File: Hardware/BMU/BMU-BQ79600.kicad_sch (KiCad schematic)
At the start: 9 parts, among them U4 BQ79600PWRQ1

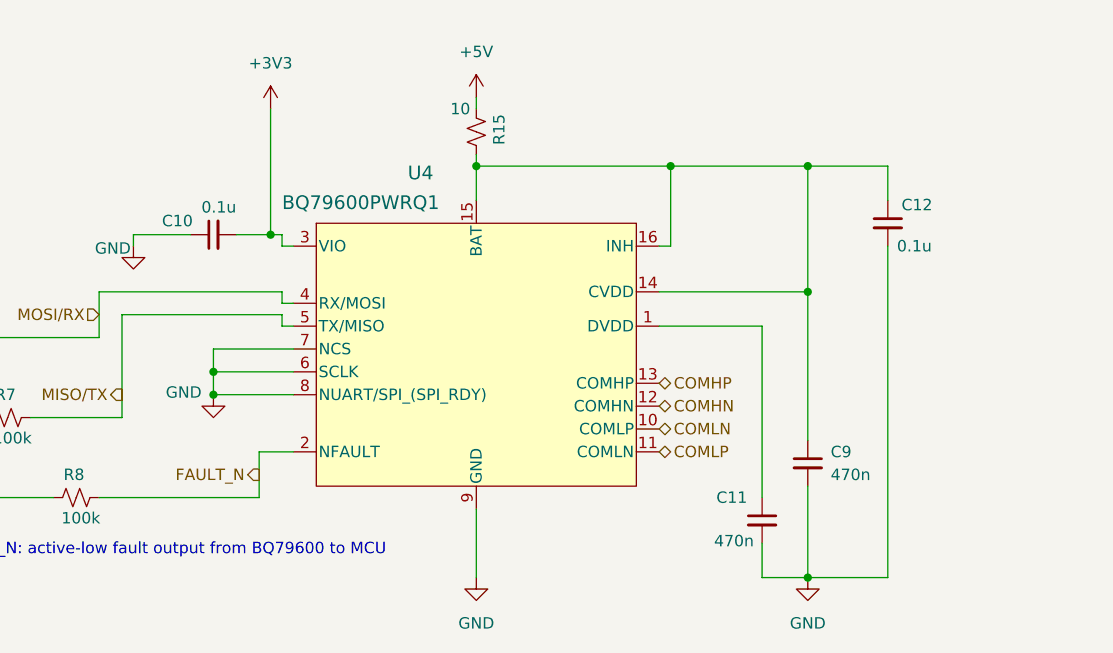
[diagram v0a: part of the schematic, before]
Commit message: change CAN
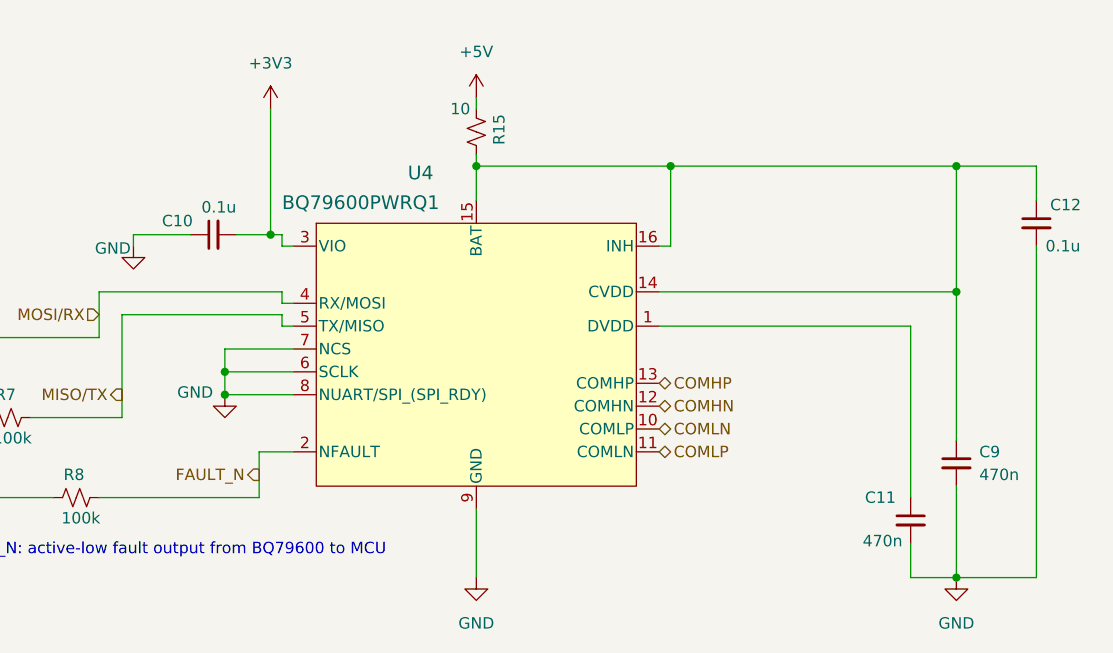
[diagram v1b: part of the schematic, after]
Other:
- moved on the sheet: C11, C12, C9

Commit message: add comment
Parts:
- C11, C9: value 470n -> 0.22u
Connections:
- net COMLN: now also U4.11 (COMLN); no longer U4.10 (COMLP)
- net COMLP: now also U4.10 (COMLP); no longer U4.11 (COMLN)
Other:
- note added: "Differential daisy-chain communication pair (H side)"
- note added: "Differential daisy-chain communication pair (L side)"
- note added: "FAULT_N: active-low fault output from BQ79600 to MCU"
- note added: "Ring architecture reserved: both COMH and COML pairs are routed out"
- note added: "nCS+SCLK: Tied to GND in UART mode"
- note added: "nUART/SPI: Mode select pin; tied to GND for UART mode"
- note removed: "BQ_FAULT_N: active-low fault output from BQ79600 to MCU"
- moved on the sheet: C10, C11, C12, C9, R15, R7, R8, R9, U4

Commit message: add footprint
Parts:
- C10, C11, C12, C9: footprint (none) -> Capacitor_SMD:C_0805_2012Metric
- R15, R7, R8, R9: footprint (none) -> Resistor_SMD:R_0805_2012Metric
- U4: footprint TSSOP16_PW_TEX -> BQ79600:TSSOP16_PW_TEX
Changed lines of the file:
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@@
 			)
 		)
-		(property "Footprint" ""
+		(property "Footprint" "Resistor_SMD:R_0805_2012Metric"
 			(at 201.93 118.11 0)
 			(hide yes)
@@
 			)
 		)
-		(property "Footprint" ""
+		(property "Footprint" "Resistor_SMD:R_0805_2012Metric"
 			(at 146.05 140.97 0)
 			(hide yes)
@@
 			)
 		)
-		(property "Footprint" ""
+		(property "Footprint" "Capacitor_SMD:C_0805_2012Metric"
 			(at 241.3 157.48 0)
 			(hide yes)
@@
 			)
 		)
-		(property "Footprint" ""
+		(property "Footprint" "Capacitor_SMD:C_0805_2012Metric"
 			(at 172.72 125.73 0)
 			(hide yes)
@@
 			)
 		)
-		(property "Footprint" "TSSOP16_PW_TEX"
+		(property "Footprint" "BQ79600:TSSOP16_PW_TEX"
 			(at 173.99 132.08 0)
 			(hide yes)
@@
 			)
 		)
-		(property "Footprint" ""
+		(property "Footprint" "Resistor_SMD:R_0805_2012Metric"
 			(at 149.86 149.86 0)
 			(hide yes)
@@
 			)
 		)
-		(property "Footprint" ""
+		(property "Footprint" "Capacitor_SMD:C_0805_2012Metric"
 			(at 255.27 132.08 0)
 			(hide yes)
@@
 			)
 		)
-		(property "Footprint" ""
+		(property "Footprint" "Resistor_SMD:R_0805_2012Metric"
 			(at 157.48 158.75 0)
 			(hide yes)
@@
 			)
 		)
-		(property "Footprint" ""
+		(property "Footprint" "Capacitor_SMD:C_0805_2012Metric"
 			(at 246.38 148.59 0)
 			(hide yes)

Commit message: add iso
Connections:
- net COMHN: no longer U4.12 (COMHN)
- net COMHP: no longer U4.13 (COMHP)
- net COMLN: no longer U4.11 (COMLN)
- net COMLP: no longer U4.10 (COMLP)
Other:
- note added: "ISO"
- moved on the sheet: C10, C11, C12, C9, R15, R7, R8, R9, U4
